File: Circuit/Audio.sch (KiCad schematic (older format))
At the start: 16 parts, among them U5 NAU8814

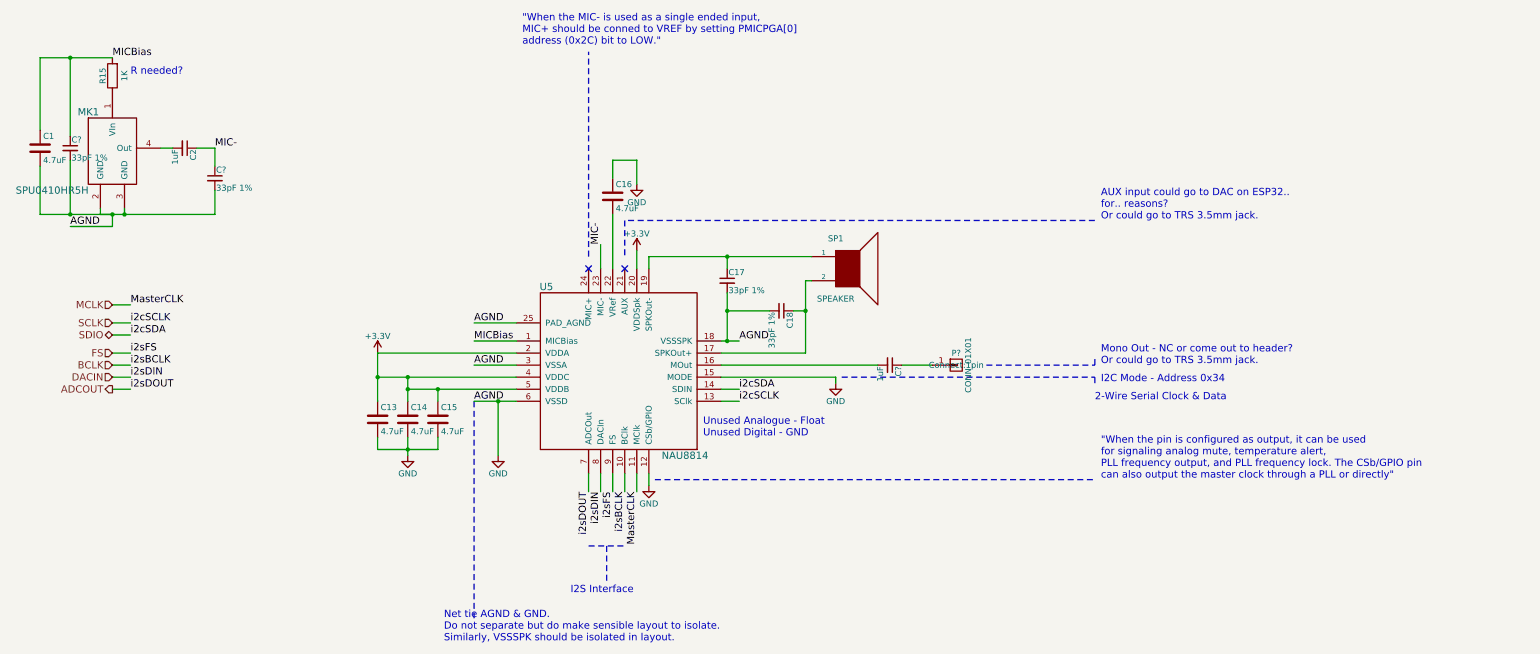
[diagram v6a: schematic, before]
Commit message: Added 3.5mm jack and header pin to audio schematic.
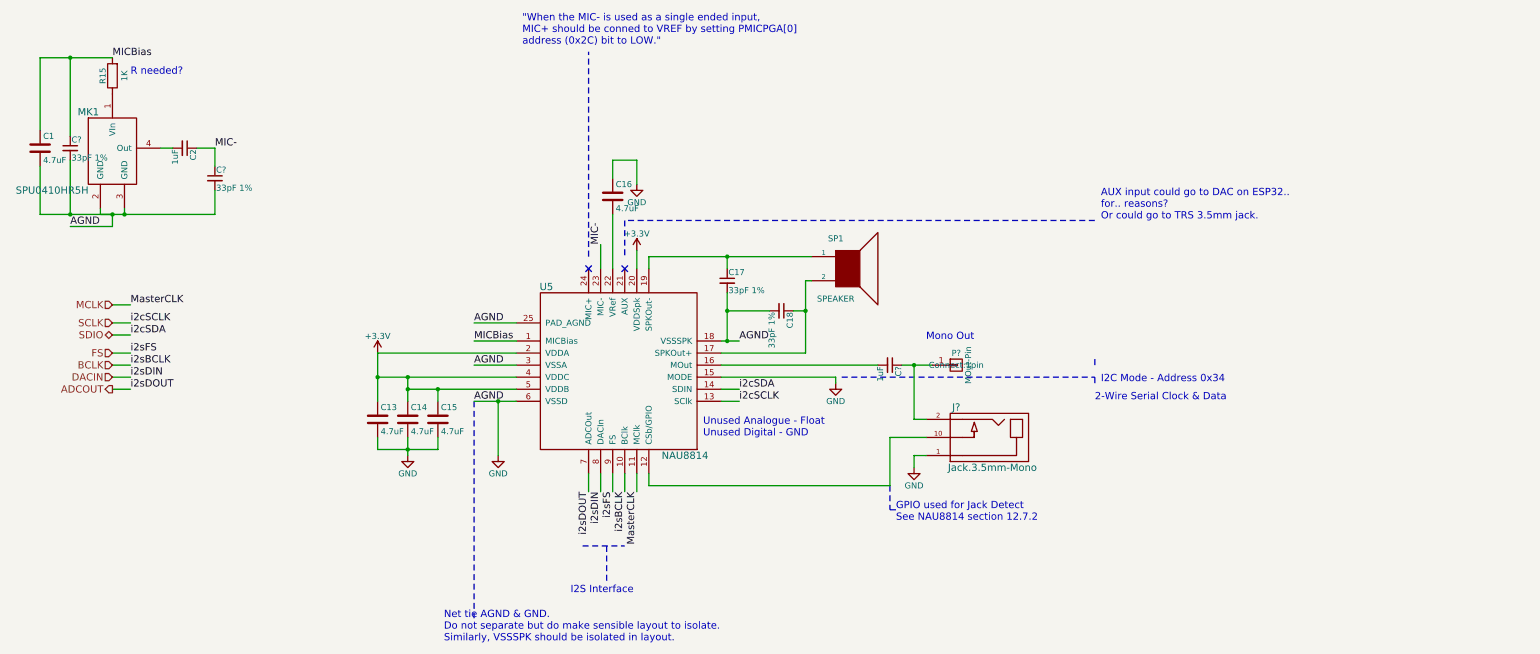
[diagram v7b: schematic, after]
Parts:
- added J?: Jack.3.5mm-Mono, symbol Jack.3.5mm-Mono
- P?: value CONN_01X01 -> MOut-Pin
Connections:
- net GND: now also J?.1; no longer U5.12 (CSb/GPIO)
- net at C?.1, P?.1 (P1): now also J?.2
- new net: J?.10, U5.12 (CSb/GPIO)
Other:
- note added: "GPIO used for Jack Detect\nSee NAU8814 section 12.7.2"
- note added: "Mono Out"
- note removed: ""When the pin is configured as output, it can be used\nfor signaling analog mute, temperature alert, \nPLL frequency output, and PLL frequency lock. The CSb/GPIO pin\ncan also output the master clock through a PLL or directly""
- note removed: "Mono Out - NC or come out to header?\nOr could go to TRS 3.5mm jack."
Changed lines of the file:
@@
 LIBS:ili9341.touchlcd.red
 LIBS:NCP5501
+LIBS:Jack.3.5mm-CUI-MJ3523
 LIBS:IoTuz-cache
 EELAYER 25 0
@@
 	1300 2400 1300 2450
 Wire Wire Line
-	1300 2450 2250 2450
+	1300 2450 1400 2450
+Wire Wire Line
+	1400 2450 1500 2450
+Wire Wire Line
+	1500 2450 2250 2450
 Wire Wire Line
 	1400 2550 1400 2450
@@
 AGND
 Wire Wire Line
-	6450 3500 6600 3500
+	6450 3500 6500 3500
+Wire Wire Line
+	6500 3500 6600 3500
 $Comp
 L C C16
@@
 $EndComp
 Wire Wire Line
-	800  1150 1400 1150
+	800  1150 1050 1150
+Wire Wire Line
+	1050 1150 1400 1150
 Wire Wire Line
 	800  1150 800  1750
 Wire Wire Line
-	1400 2450 800  2450
+	1400 2450 1050 2450
+Wire Wire Line
+	1050 2450 800  2450
 Wire Wire Line
 	800  2450 800  2050
@@
 NoConn ~ 5650 2900
 Wire Wire Line
-	5850 2800 7200 2800
+	5850 2800 6500 2800
+Wire Wire Line
+	6500 2800 7200 2800
 Wire Wire Line
 	5850 2800 5850 2900
@@
 	7200 3000 7150 3000
 Wire Wire Line
-	7150 3000 7150 3600
+	7150 3000 7150 3250
+Wire Wire Line
+	7150 3250 7150 3600
 Wire Wire Line
 	7150 3600 6450 3600
-Text Notes 9600 3700 0    60   ~ 0
-Mono Out - NC or come out to header?\nOr could go to TRS 3.5mm jack.
 $Comp
 L GND #PWR54
@@
 $EndComp
 Wire Wire Line
-	4400 4000 4750 4000
+	4400 4000 4600 4000
+Wire Wire Line
+	4600 4000 4750 4000
 Wire Wire Line
 	4600 4000 4600 4450
@@
 Net tie AGND & GND. \nDo not separate but do make sensible layout to isolate.\nSimilarly, VSSSPK should be isolated in layout.
 Wire Wire Line
-	3850 3900 4750 3900
+	3850 3900 4100 3900
+Wire Wire Line
+	4100 3900 4750 3900
 Wire Wire Line
 	4100 3900 4100 4000
 Wire Wire Line
-	3600 3800 4750 3800
-Wire Wire Line
-	3850 3800 3850 4000
+	3600 3800 3850 3800
+Wire Wire Line
+	3850 3800 4750 3800
+Wire Wire Line
+	3850 3800 3850 3900
+Wire Wire Line
+	3850 3900 3850 4000
 Wire Wire Line
 	4750 3600 3600 3600
 Wire Wire Line
-	3600 3600 3600 4000
+	3600 3600 3600 3800
+Wire Wire Line
+	3600 3800 3600 4000
 Connection ~ 3850 3900
 Connection ~ 4100 3900
@@
 $EndComp
 Wire Wire Line
-	3850 4300 3850 4450
-Wire Wire Line
-	3600 4400 4100 4400
+	3850 4300 3850 4400
+Wire Wire Line
+	3850 4400 3850 4450
+Wire Wire Line
+	3600 4400 3850 4400
+Wire Wire Line
+	3850 4400 4100 4400
 Wire Wire Line
 	4100 4400 4100 4300
@@
 L GND #PWR57
 U 1 1 581C0598
-P 5850 4700
-F 0 "#PWR57" H 5850 4450 50  0001 C CNN
-F 1 "GND" H 5850 4550 50  0000 C CNN
-F 2 "" H 5850 4700 50  0000 C CNN
-F 3 "" H 5850 4700 50  0000 C CNN
-	1    5850 4700
+P 8050 4550
+F 0 "#PWR57" H 8050 4300 50  0001 C CNN
+F 1 "GND" H 8050 4400 50  0000 C CNN
+F 2 "" H 8050 4550 50  0000 C CNN
+F 3 "" H 8050 4550 50  0000 C CNN
+	1    8050 4550
 	1    0    0    -1
 $EndComp
 Wire Wire Line
 	5850 4700 5850 4600
-Wire Notes Line
-	5900 4650 9550 4650
-Text Notes 9600 4650 0    60   ~ 0
-"When the pin is configured as output, it can be used\nfor signaling analog mute, temperature alert, \nPLL frequency output, and PLL frequency lock. The CSb/GPIO pin\ncan also output the master clock through a PLL or directly"
 Text Notes 9550 4000 0    60   ~ 0
  2-Wire Serial Clock & Data
 Wire Notes Line
-	5350 5200 5650 5200
+	5300 5200 5650 5200
 Text HLabel 1400 3200 0    60   Input ~ 0
 MCLK
@@
 	6850 3250 6500 3250
 Wire Wire Line
-	6500 3100 6500 3500
+	6500 3100 6500 3250
+Wire Wire Line
+	6500 3250 6500 3500
 Connection ~ 6500 3500
 Connection ~ 6500 3250
@@
 P 8400 3700
 F 0 "P?" H 8400 3800 50  0000 C CNN
-F 1 "CONN_01X01" V 8500 3700 50  0000 C CNN
+F 1 "MOut-Pin" V 8500 3700 50  0000 C CNN
 F 2 "Connect:1pin" H 8400 3700 50  0000 C CNN
 F 3 "" H 8400 3700 50  0000 C CNN
@@
 $EndComp
 Wire Wire Line
-	7950 3700 8200 3700
-Wire Notes Line
-	8650 3700 9550 3700
+	7950 3700 8050 3700
+Wire Wire Line
+	8050 3700 8200 3700
 Wire Notes Line
 	9550 3700 9550 3650
+$Comp
+L Jack.3.5mm-Mono J?
+U 1 1 5826FDD0
+P 8650 4300
+F 0 "J?" H 8900 4050 60  0000 C CNN
+F 1 "Jack.3.5mm-Mono" H 8600 4550 60  0000 C CNN
+F 2 "" H 8650 4350 60  0001 C CNN
+F 3 "" H 8650 4350 60  0001 C CNN
+	1    8650 4300
+	-1   0    0    1
+$EndComp
+Wire Wire Line
+	5850 4700 7850 4700
+Wire Wire Line
+	7850 4700 7850 4300
+Wire Wire Line
+	7850 4300 8150 4300
+Wire Wire Line
+	8150 4450 8050 4450
+Wire Wire Line
+	8050 4450 8050 4550
+Wire Wire Line
+	8050 3700 8050 4150
+Wire Wire Line
+	8050 4150 8150 4150
+Connection ~ 8050 3700
+Text Notes 7900 5000 0    60   ~ 0
+GPIO used for Jack Detect\nSee NAU8814 section 12.7.2
+Wire Notes Line
+	7850 4700 7850 4900
+Wire Notes Line
+	7850 4900 7900 4900
+Text Notes 8150 3500 0    60   ~ 0
+Mono Out
 $EndSCHEMATC

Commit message: Alligator pads & more audio.
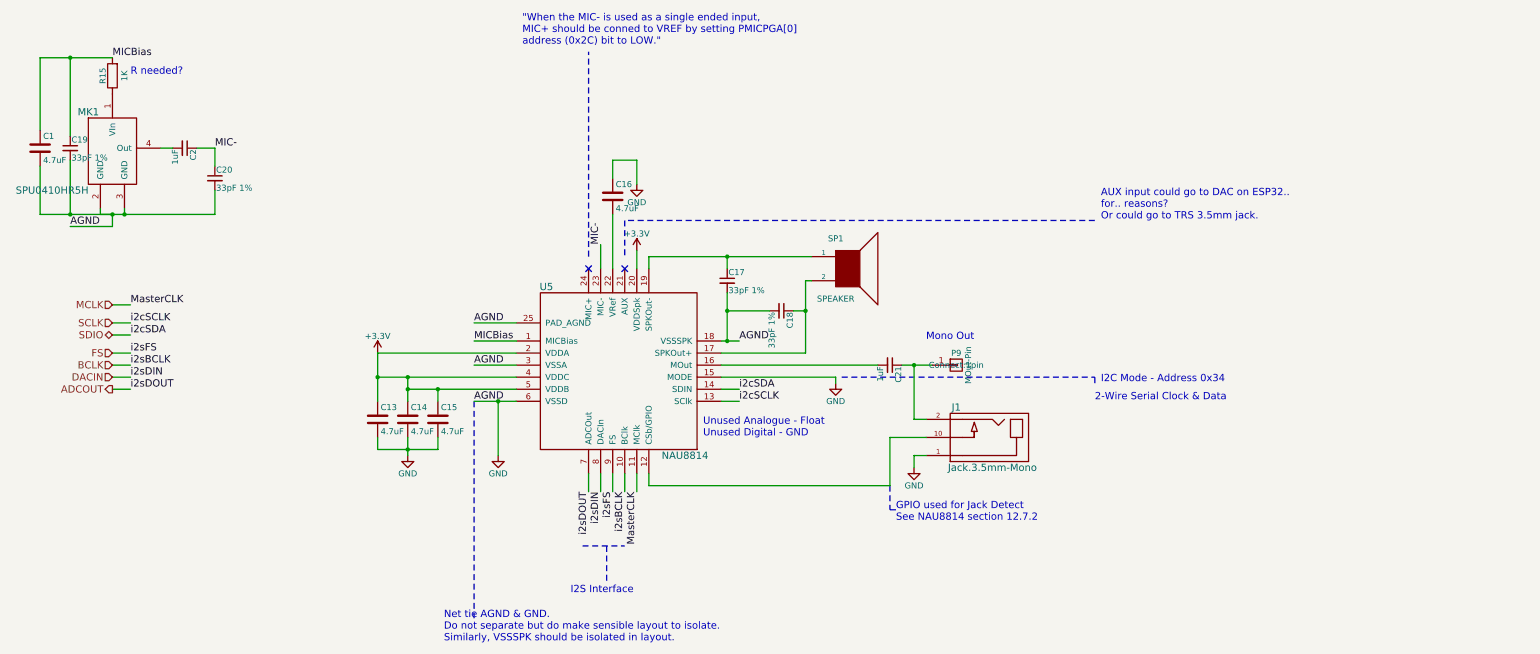
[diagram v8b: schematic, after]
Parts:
- J1: renamed from J?; footprint (none) -> libs:3.5mmMonoTRSJack.MJ-3523-SMT.Switch; Digikey PN (none) -> CP-3523MJCT-ND; Link (none) -> http://www.digikey.com.au/product-detail/en/cui-inc/MJ-3523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; Manufacturer PN (none) -> MJ-3523-SMT-TR; Unit Cost (none) -> 1.34
- gave numbers to parts that had none: 4
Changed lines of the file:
@@
 	1300 2400 1300 2450
 Wire Wire Line
-	1300 2450 1400 2450
-Wire Wire Line
-	1400 2450 1500 2450
-Wire Wire Line
-	1500 2450 2250 2450
+	1300 2450 2250 2450
 Wire Wire Line
 	1400 2550 1400 2450
@@
 Connection ~ 1400 2450
 $Comp
-L +3.3V #PWR56
+L +3.3V #PWR057
 U 1 1 581BE27A
 P 5750 2750
-F 0 "#PWR56" H 5750 2600 50  0001 C CNN
+F 0 "#PWR057" H 5750 2600 50  0001 C CNN
 F 1 "+3.3V" H 5750 2890 50  0000 C CNN
 F 2 "" H 5750 2750 50  0000 C CNN
@@
 AGND
 Wire Wire Line
-	6450 3500 6500 3500
-Wire Wire Line
-	6500 3500 6600 3500
+	6450 3500 6600 3500
 $Comp
 L C C16
@@
 	2100 1900 2250 1900
 $Comp
-L GND #PWR55
+L GND #PWR058
 U 1 1 581BEFAA
 P 5750 2200
-F 0 "#PWR55" H 5750 1950 50  0001 C CNN
+F 0 "#PWR058" H 5750 1950 50  0001 C CNN
 F 1 "GND" H 5750 2050 50  0000 C CNN
 F 2 "" H 5750 2200 50  0000 C CNN
@@
 $EndComp
 Wire Wire Line
-	800  1150 1050 1150
-Wire Wire Line
-	1050 1150 1400 1150
+	800  1150 1400 1150
 Wire Wire Line
 	800  1150 800  1750
 Wire Wire Line
-	1400 2450 1050 2450
-Wire Wire Line
-	1050 2450 800  2450
+	1400 2450 800  2450
 Wire Wire Line
 	800  2450 800  2050
 $Comp
-L GND #PWR58
+L GND #PWR059
 U 1 1 581BF41C
 P 7400 3850
-F 0 "#PWR58" H 7400 3600 50  0001 C CNN
+F 0 "#PWR059" H 7400 3600 50  0001 C CNN
 F 1 "GND" H 7400 3700 50  0000 C CNN
 F 2 "" H 7400 3850 50  0000 C CNN
@@
 NoConn ~ 5650 2900
 Wire Wire Line
-	5850 2800 6500 2800
-Wire Wire Line
-	6500 2800 7200 2800
+	5850 2800 7200 2800
 Wire Wire Line
 	5850 2800 5850 2900
@@
 	7200 3000 7150 3000
 Wire Wire Line
-	7150 3000 7150 3250
-Wire Wire Line
-	7150 3250 7150 3600
+	7150 3000 7150 3600
 Wire Wire Line
 	7150 3600 6450 3600
 $Comp
-L GND #PWR54
+L GND #PWR060
 U 1 1 581BFD59
 P 4600 4450
-F 0 "#PWR54" H 4600 4200 50  0001 C CNN
+F 0 "#PWR060" H 4600 4200 50  0001 C CNN
 F 1 "GND" H 4600 4300 50  0000 C CNN
 F 2 "" H 4600 4450 50  0000 C CNN
@@
 $EndComp
 Wire Wire Line
-	4400 4000 4600 4000
-Wire Wire Line
-	4600 4000 4750 4000
+	4400 4000 4750 4000
 Wire Wire Line
 	4600 4000 4600 4450
@@
 Net tie AGND & GND. \nDo not separate but do make sensible layout to isolate.\nSimilarly, VSSSPK should be isolated in layout.
 Wire Wire Line
-	3850 3900 4100 3900
-Wire Wire Line
-	4100 3900 4750 3900
+	3850 3900 4750 3900
 Wire Wire Line
 	4100 3900 4100 4000
 Wire Wire Line
-	3600 3800 3850 3800
-Wire Wire Line
-	3850 3800 4750 3800
-Wire Wire Line
-	3850 3800 3850 3900
-Wire Wire Line
-	3850 3900 3850 4000
+	3600 3800 4750 3800
+Wire Wire Line
+	3850 3800 3850 4000
 Wire Wire Line
 	4750 3600 3600 3600
 Wire Wire Line
-	3600 3600 3600 3800
-Wire Wire Line
-	3600 3800 3600 4000
+	3600 3600 3600 4000
 Connection ~ 3850 3900
 Connection ~ 4100 3900
@@
 Connection ~ 3850 3800
 $Comp
-L +3.3V #PWR52
+L +3.3V #PWR061
 U 1 1 581C0164
 P 3600 3600
-F 0 "#PWR52" H 3600 3450 50  0001 C CNN
+F 0 "#PWR061" H 3600 3450 50  0001 C CNN
 F 1 "+3.3V" H 3600 3740 50  0000 C CNN
 F 2 "" H 3600 3600 50  0000 C CNN
@@
 $EndComp
 $Comp
-L GND #PWR53
+L GND #PWR062
 U 1 1 581C01A1
 P 3850 4450
-F 0 "#PWR53" H 3850 4200 50  0001 C CNN
+F 0 "#PWR062" H 3850 4200 50  0001 C CNN
 F 1 "GND" H 3850 4300 50  0000 C CNN
 F 2 "" H 3850 4450 50  0000 C CNN
@@
 $EndComp
 Wire Wire Line
-	3850 4300 3850 4400
-Wire Wire Line
-	3850 4400 3850 4450
-Wire Wire Line
-	3600 4400 3850 4400
-Wire Wire Line
-	3850 4400 4100 4400
+	3850 4300 3850 4450
+Wire Wire Line
+	3600 4400 4100 4400
 Wire Wire Line
 	4100 4400 4100 4300
@@
 AUX input could go to DAC on ESP32..\nfor.. reasons?\nOr could go to TRS 3.5mm jack.
 $Comp
-L GND #PWR57
+L GND #PWR063
 U 1 1 581C0598
 P 8050 4550
-F 0 "#PWR57" H 8050 4300 50  0001 C CNN
+F 0 "#PWR063" H 8050 4300 50  0001 C CNN
 F 1 "GND" H 8050 4400 50  0000 C CNN
 F 2 "" H 8050 4550 50  0000 C CNN
@@
 	6850 3250 6500 3250
 Wire Wire Line
-	6500 3100 6500 3250
-Wire Wire Line
-	6500 3250 6500 3500
+	6500 3100 6500 3500
 Connection ~ 6500 3500
 Connection ~ 6500 3250
@@
 $EndComp
 $Comp
-L C_Small C?
+L C_Small C19
 U 1 1 582BA612
 P 1050 1900
-F 0 "C?" H 1060 1970 50  0000 L CNN
+F 0 "C19" H 1060 1970 50  0000 L CNN
 F 1 "33pF 1%" H 1060 1820 50  0000 L CNN
 F 2 "Capacitors_SMD:C_0603_HandSoldering" H 1050 1900 50  0001 C CNN
@@
 $EndComp
 $Comp
-L C_Small C?
+L C_Small C20
 U 1 1 582BA791
 P 2250 2150
-F 0 "C?" H 2260 2220 50  0000 L CNN
+F 0 "C20" H 2260 2220 50  0000 L CNN
 F 1 "33pF 1%" H 2260 2070 50  0000 L CNN
 F 2 "Capacitors_SMD:C_0603_HandSoldering" H 2250 2150 50  0001 C CNN
@@
 $EndComp
 $Comp
-L C_Small C?
+L C_Small C21
 U 1 1 582BA940
 P 7850 3700
-F 0 "C?" H 7860 3770 50  0000 L CNN
+F 0 "C21" H 7860 3770 50  0000 L CNN
 F 1 "1uF" H 7860 3620 50  0000 L CNN
 F 2 "Capacitors_SMD:C_0603_HandSoldering" H 7850 3700 50  0001 C CNN
@@
 	2250 2450 2250 2250
 $Comp
-L CONN_01X01 P?
+L CONN_01X01 P9
 U 1 1 582BB613
 P 8400 3700
-F 0 "P?" H 8400 3800 50  0000 C CNN
+F 0 "P9" H 8400 3800 50  0000 C CNN
 F 1 "MOut-Pin" V 8500 3700 50  0000 C CNN
 F 2 "Connect:1pin" H 8400 3700 50  0000 C CNN
@@
 $EndComp
 Wire Wire Line
-	7950 3700 8050 3700
-Wire Wire Line
-	8050 3700 8200 3700
-Wire Notes Line
-	9550 3700 9550 3650
-$Comp
-L Jack.3.5mm-Mono J?
+	7950 3700 8200 3700
+$Comp
+L Jack.3.5mm-Mono J1
 U 1 1 5826FDD0
 P 8650 4300
-F 0 "J?" H 8900 4050 60  0000 C CNN
+F 0 "J1" H 8900 4050 60  0000 C CNN
 F 1 "Jack.3.5mm-Mono" H 8600 4550 60  0000 C CNN
-F 2 "" H 8650 4350 60  0001 C CNN
+F 2 "libs:3.5mmMonoTRSJack.MJ-3523-SMT.Switch" H 8650 4350 60  0001 C CNN
 F 3 "" H 8650 4350 60  0001 C CNN
+F 4 "CP-3523MJCT-ND" H 8650 4300 60  0001 C CNN "Digikey PN"
+F 5 "http://www.digikey.com.au/product-detail/en/cui-inc/MJ-3523-SMT-TR/CP-3523MJCT-ND/669691" H 8650 4300 60  0001 C CNN "Link"
+F 6 "MJ-3523-SMT-TR" H 8650 4300 60  0001 C CNN "Manufacturer PN"
+F 7 "1.34" H 8650 4300 60  0001 C CNN "Unit Cost"
 	1    8650 4300
 	-1   0    0    1
